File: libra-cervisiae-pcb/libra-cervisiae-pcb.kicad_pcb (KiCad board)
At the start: 2 copper layers, 63.8 x 43.2 mm, 159 parts, among them CN1 CP2102, CN3 HX711_BREAKOUT, J1 Board Temp, J10 Load Cell, J12 Load Cell, J4 Wort Temp, J8 Load Cell, J9 Load Cell, SW1 Reset, SW2 Flash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

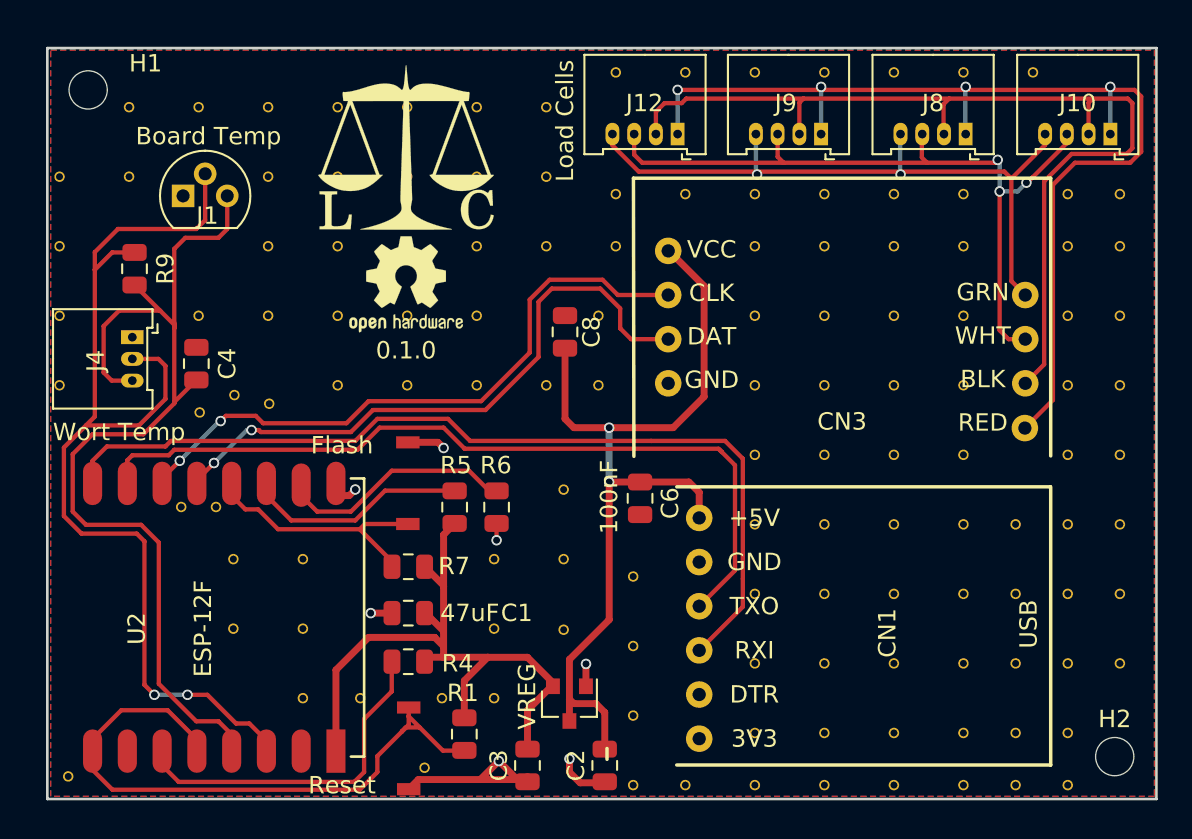
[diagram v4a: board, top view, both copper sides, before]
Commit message: Measure HX711 with calibers, update footprint, PCB 0.1.1
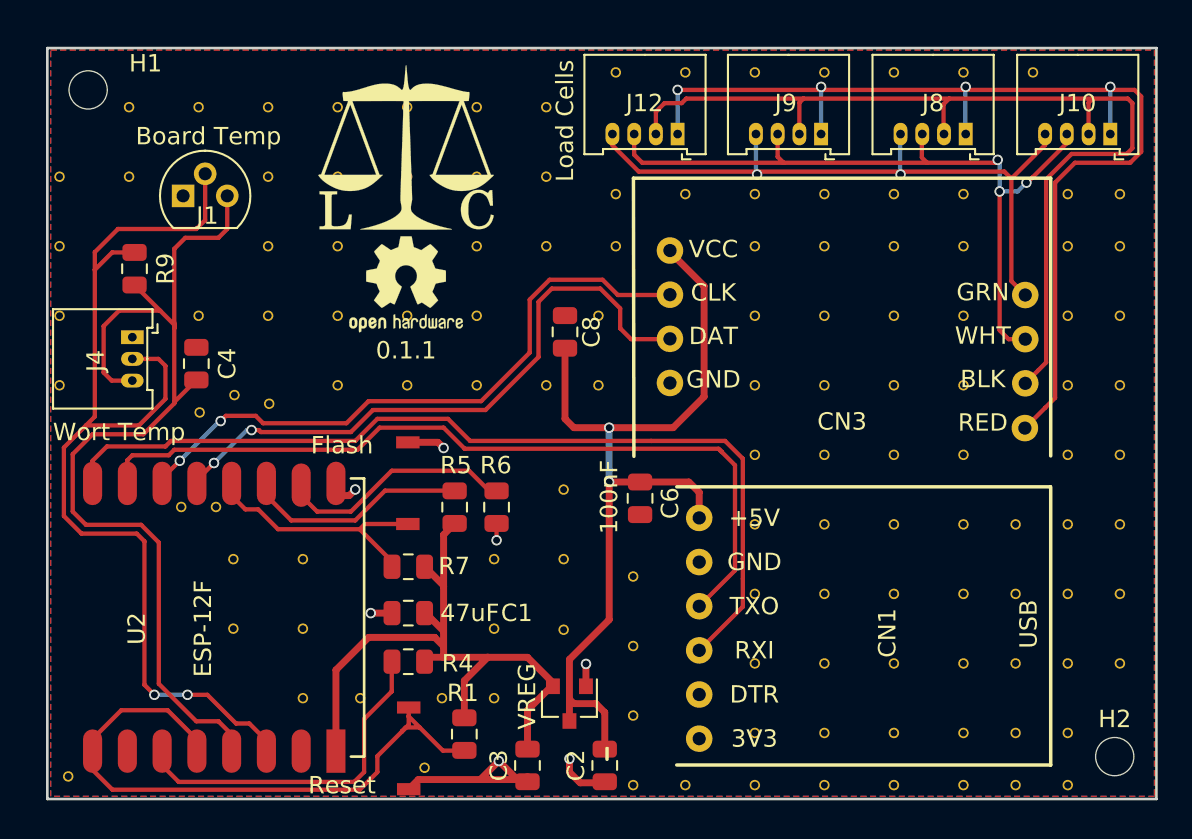
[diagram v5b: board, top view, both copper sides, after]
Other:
- board text added: "0.1.1"
- board text removed: "0.1.0"
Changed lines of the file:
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@@
     (thickness 1.6)
     (drawings 17)
-    (tracks 336)
+    (tracks 337)
     (zones 0)
     (modules 159)
@@
   (title_block
     (title "Libra Cervisiae PCB")
-    (date 2018-07-23)
-    (rev 0.1.0)
+    (date 2018-08-05)
+    (rev 0.1.1)
   )
   (layers
@@
     (add_net "Net-(R6-Pad2)")
   )
+  (module HX711:HX711-MINI (layer F.Cu)
+    (at 139.954 73.025)
+    (fp_text reference CN3 (at 12 14) (layer F.SilkS)
+      (effects (font (size 1 1) (thickness 0.15)))
+    )
+    (fp_text value HX711_BREAKOUT (at 10.5 1) (layer F.Fab)
+      (effects (font (size 1 1) (thickness 0.15)))
+    )
+    (fp_line (start 0 16) (end 0 0) (layer F.Fab) (width 0.1))
+    (fp_line (start 24 0) (end 24 16) (layer F.Fab) (width 0.1))
+    (fp_line (start 0 0) (end 24 0) (layer F.Fab) (width 0.1))
+    (fp_line (start 0 16) (end 24 16) (layer F.Fab) (width 0.1))
+    (fp_text user VCC (at 4.6 4.08) (layer F.SilkS)
+      (effects (font (size 1 1) (thickness 0.15)))
+    )
+    (fp_text user CLK (at 4.6 6.58) (layer F.SilkS)
+      (effects (font (size 1 1) (thickness 0.15)))
+    )
+    (fp_text user DAT (at 4.6 9.08) (layer F.SilkS)
+      (effects (font (size 1 1) (thickness 0.15)))
+    )
+    (fp_text user GND (at 4.6 11.58) (layer F.SilkS)
+      (effects (font (size 1 1) (thickness 0.15)))
+    )
+    (fp_text user GRN (at 20.1 6.56) (layer F.SilkS)
+      (effects (font (size 1 1) (thickness 0.15)))
+    )
+    (fp_text user WHT (at 20.1 9.06) (layer F.SilkS)
+      (effects (font (size 1 1) (thickness 0.15)))
+    )
+    (fp_text user BLK (at 20.1 11.56) (layer F.SilkS)
+      (effects (font (size 1 1) (thickness 0.15)))
+    )
+    (fp_text user RED (at 20.1 14.06) (layer F.SilkS)
+      (effects (font (size 1 1) (thickness 0.15)))
+    )
+    (pad 2 thru_hole circle (at 22.54 11.8) (size 1.524 1.524) (drill 0.762) (layers *.Cu *.Mask)
+      (net 13 /E-))
+    (pad 3 thru_hole circle (at 22.54 9.26) (size 1.524 1.524) (drill 0.762) (layers *.Cu *.Mask)
+      (net 14 /S-))
+    (pad 4 thru_hole circle (at 22.54 6.72) (size 1.524 1.524) (drill 0.762) (layers *.Cu *.Mask)
+      (net 15 /S+))
+    (pad 1 thru_hole circle (at 22.517 14.3745) (size 1.524 1.524) (drill 0.762) (layers *.Cu *.Mask)
+      (net 16 /E+))
+    (pad 10 thru_hole circle (at 2.1 11.78) (size 1.524 1.524) (drill 0.762) (layers *.Cu *.Mask)
+      (net 6 /GND))
+    (pad 8 thru_hole circle (at 2.1 9.24) (size 1.524 1.524) (drill 0.762) (layers *.Cu *.Mask)
+      (net 9 /DAT))
+    (pad 9 thru_hole circle (at 2.1 6.7) (size 1.524 1.524) (drill 0.762) (layers *.Cu *.Mask)
+      (net 10 /CLK))
+    (pad 7 thru_hole circle (at 2.1 4.16) (size 1.524 1.524) (drill 0.762) (layers *.Cu *.Mask)
+      (net 7 /USB+))
+  )
   (module Extra_Pads:Stitching_Via_0.6mm (layer F.Cu)
     (at 119 86)
@@
     (pad 1 thru_hole circle (at 20.22 1.54 180) (size 1.524 1.524) (drill 0.762) (layers *.Cu *.Mask))
   )
-  (module HX711:HX711-MINI (layer F.Cu)
-    (at 139.954 73.025)
-    (fp_text reference CN3 (at 12 14) (layer F.SilkS)
-      (effects (font (size 1 1) (thickness 0.15)))
-    )
-    (fp_text value HX711_BREAKOUT (at 10.5 1) (layer F.Fab)
-      (effects (font (size 1 1) (thickness 0.15)))
-    )
-    (fp_line (start 0 16) (end 0 0) (layer F.Fab) (width 0.1))
-    (fp_line (start 24 0) (end 24 16) (layer F.Fab) (width 0.1))
-    (fp_line (start 0 0) (end 24 0) (layer F.Fab) (width 0.1))
-    (fp_line (start 0 16) (end 24 16) (layer F.Fab) (width 0.1))
-    (fp_text user VCC (at 4.5 4.1) (layer F.SilkS)
-      (effects (font (size 1 1) (thickness 0.15)))
-    )
-    (fp_text user CLK (at 4.5 6.6) (layer F.SilkS)
-      (effects (font (size 1 1) (thickness 0.15)))
-    )
-    (fp_text user DAT (at 4.5 9.1) (layer F.SilkS)
-      (effects (font (size 1 1) (thickness 0.15)))
-    )
-    (fp_text user GND (at 4.5 11.6) (layer F.SilkS)
-      (effects (font (size 1 1) (thickness 0.15)))
-    )
-    (fp_text user GRN (at 20.1 6.56) (layer F.SilkS)
-      (effects (font (size 1 1) (thickness 0.15)))
-    )
-    (fp_text user WHT (at 20.1 9.06) (layer F.SilkS)
-      (effects (font (size 1 1) (thickness 0.15)))
-    )
-    (fp_text user BLK (at 20.1 11.56) (layer F.SilkS)
-      (effects (font (size 1 1) (thickness 0.15)))
-    )
-    (fp_text user RED (at 20.1 14.06) (layer F.SilkS)
-      (effects (font (size 1 1) (thickness 0.15)))
-    )
-    (pad 2 thru_hole circle (at 22.54 11.8) (size 1.524 1.524) (drill 0.762) (layers *.Cu *.Mask)
-      (net 13 /E-))
-    (pad 3 thru_hole circle (at 22.54 9.26) (size 1.524 1.524) (drill 0.762) (layers *.Cu *.Mask)
-      (net 14 /S-))
-    (pad 4 thru_hole circle (at 22.54 6.72) (size 1.524 1.524) (drill 0.762) (layers *.Cu *.Mask)
-      (net 15 /S+))
-    (pad 1 thru_hole circle (at 22.517 14.3745) (size 1.524 1.524) (drill 0.762) (layers *.Cu *.Mask)
-      (net 16 /E+))
-    (pad 10 thru_hole circle (at 2 11.8) (size 1.524 1.524) (drill 0.762) (layers *.Cu *.Mask)
-      (net 6 /GND))
-    (pad 8 thru_hole circle (at 2 9.26) (size 1.524 1.524) (drill 0.762) (layers *.Cu *.Mask)
-      (net 9 /DAT))
-    (pad 9 thru_hole circle (at 2 6.72) (size 1.524 1.524) (drill 0.762) (layers *.Cu *.Mask)
-      (net 10 /CLK))
-    (pad 7 thru_hole circle (at 2 4.18) (size 1.524 1.524) (drill 0.762) (layers *.Cu *.Mask)
-      (net 7 /USB+))
-  )
   (module Connector_Molex:Molex_PicoBlade_53048-0810_1x04_P1.25mm_Horizontal (layer F.Cu)
     (at 159.0675 70.485 180)
@@
     (arrow2b (pts (xy 100.138 111.738) (xy 101.264504 111.151579)))
   )
-  (gr_text 0.1.0 (at 126.873 82.931) (layer F.SilkS)
+  (gr_text 0.1.1 (at 126.873 82.931) (layer F.SilkS)
     (effects (font (size 1 1) (thickness 0.15)))
   )
@@
   (segment (start 157.794 70.104) (end 157.794 68.76601) (width 0.25) (layer F.Cu) (net 13) (status 10))
   (segment (start 166.37 68.44501) (end 158.115 68.44501) (width 0.25) (layer F.Cu) (net 13))
-  (segment (start 163.581001 83.737999) (end 162.494 84.825) (width 0.25) (layer F.Cu) (net 13) (status 20))
-  (segment (start 163.581001 73.203721) (end 163.581001 83.737999) (width 0.25) (layer F.Cu) (net 13))
-  (segment (start 163.58008 73.2028) (end 163.581001 73.203721) (width 0.25) (layer F.Cu) (net 13))
-  (segment (start 163.58008 73.2028) (end 165.15488 71.628) (width 0.25) (layer F.Cu) (net 13))
+  (segment (start 163.69438 83.62462) (end 163.245 84.074) (width 0.25) (layer F.Cu) (net 13))
+  (segment (start 163.69438 73.0885) (end 163.69438 83.62462) (width 0.25) (layer F.Cu) (net 13))
+  (segment (start 163.245 84.074) (end 162.494 84.825) (width 0.25) (layer F.Cu) (net 13))
+  (segment (start 163.69438 73.0885) (end 165.15488 71.628) (width 0.25) (layer F.Cu) (net 13))
   (via (at 161.019 73.787) (size 0.6) (drill 0.4) (layers F.Cu B.Cu) (net 14))
   (via (at 162.56 73.279) (size 0.6) (drill 0.4) (layers F.Cu B.Cu) (net 14))
@@
   (segment (start 150.749 70.104) (end 150.749 67.77001) (width 0.25) (layer B.Cu) (net 16) (status 10))
   (segment (start 150.749 67.77001) (end 150.749 67.945) (width 0.25) (layer F.Cu) (net 16))
-  (segment (start 164.084 73.406) (end 165.354 72.136) (width 0.25) (layer F.Cu) (net 16))
-  (segment (start 164.084 85.7865) (end 162.471 87.3995) (width 0.25) (layer F.Cu) (net 16) (status 20))
-  (segment (start 164.084 73.406) (end 164.084 85.7865) (width 0.25) (layer F.Cu) (net 16))
+  (segment (start 164.211 85.6595) (end 163.6375 86.233) (width 0.25) (layer F.Cu) (net 16))
+  (segment (start 164.211 73.279) (end 164.211 85.6595) (width 0.25) (layer F.Cu) (net 16))
+  (segment (start 163.6375 86.233) (end 162.471 87.3995) (width 0.25) (layer F.Cu) (net 16))
+  (segment (start 164.211 73.279) (end 165.354 72.136) (width 0.25) (layer F.Cu) (net 16))
   (segment (start 127.656 104.62) (end 126.856 104.62) (width 0.25) (layer F.Cu) (net 17))
   (segment (start 126.638 104.838) (end 126.638 104.8576) (width 0.25) (layer F.Cu) (net 17))
